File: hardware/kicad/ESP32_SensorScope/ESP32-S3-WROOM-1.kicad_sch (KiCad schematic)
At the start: 20 parts, among them J9 USB_C_Receptacle_USB2.0_16P, SW2 Reset, SW3 Boot, U16 TLV76133DCY, U2 ESP32-S3-WROOM-1, U27 USBLC6-2SC6

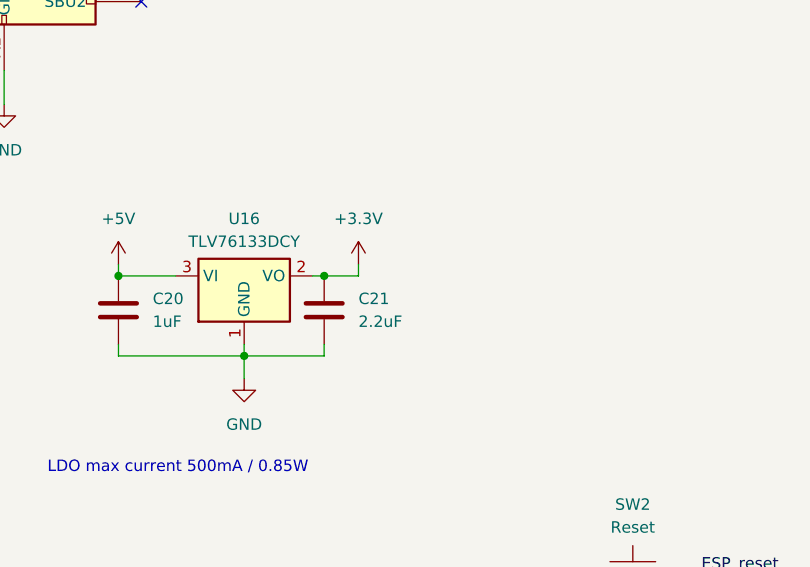
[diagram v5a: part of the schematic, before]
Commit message: addet some footprints"
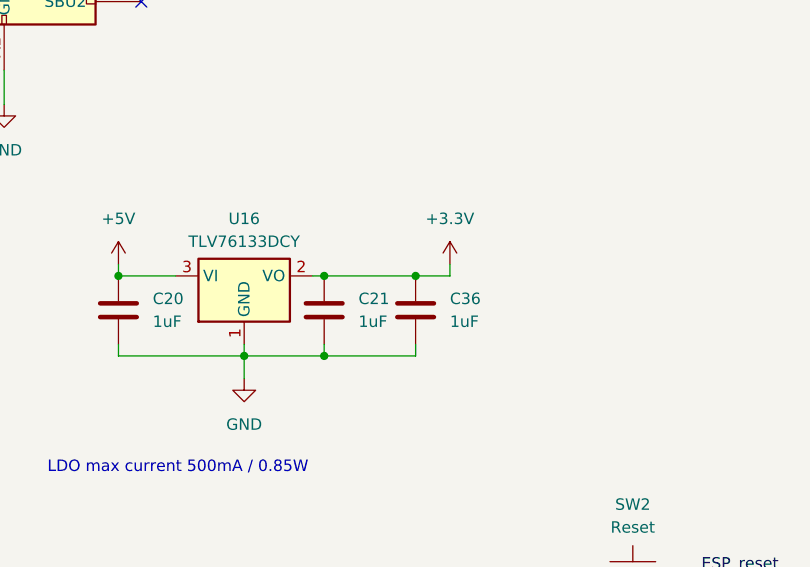
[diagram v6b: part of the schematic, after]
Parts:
- added C36: 1uF, Capacitor_SMD:C_0805_2012Metric, symbol Device:C
- C20, C22, C24: footprint (none) -> Capacitor_SMD:C_0805_2012Metric
- C21: value 2.2uF -> 1uF; footprint (none) -> Capacitor_SMD:C_0805_2012Metric
- C23: footprint (none) -> Capacitor_SMD:C_1206_3216Metric
- D11: footprint (none) -> Diode_SMD:D_SMA
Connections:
- net +3.3V: now also C36.1
- net GND: now also C36.2
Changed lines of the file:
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@@
 	(paper "A4")
 	(junction
+		(at 87.63 110.49)
+		(diameter 0)
+		(color 0 0 0 0)
+	)
+	(junction
 		(at 58.42 64.77)
 		(diameter 0)
@@
 	)
 	(junction
+		(at 77.47 119.38)
+		(diameter 0)
+		(color 0 0 0 0)
+	)
+	(junction
 		(at 77.47 110.49)
 		(diameter 0)
@@
 	(wire
 		(pts
-			(xy 77.47 110.49) (xy 81.28 110.49)
+			(xy 110.49 25.4) (xy 110.49 27.94)
 		)
 		(stroke
@@
 	(wire
 		(pts
-			(xy 110.49 25.4) (xy 110.49 27.94)
+			(xy 87.63 118.11) (xy 87.63 119.38)
+		)
+		(stroke
+			(width 0)
+			(type default)
+		)
+	)
+	(wire
+		(pts
+			(xy 87.63 119.38) (xy 77.47 119.38)
 		)
 		(stroke
@@
 	(wire
 		(pts
-			(xy 81.28 110.49) (xy 81.28 109.22)
+			(xy 91.44 110.49) (xy 91.44 109.22)
 		)
 		(stroke
@@
 	(wire
 		(pts
+			(xy 87.63 110.49) (xy 91.44 110.49)
+		)
+		(stroke
+			(width 0)
+			(type default)
+		)
+	)
+	(wire
+		(pts
 			(xy 72.39 40.64) (xy 69.85 40.64)
 		)
@@
 	(wire
 		(pts
+			(xy 77.47 110.49) (xy 87.63 110.49)
+		)
+		(stroke
+			(width 0)
+			(type default)
+		)
+	)
+	(wire
+		(pts
 			(xy 57.15 57.15) (xy 58.42 57.15)
 		)
@@
 			)
 		)
-		(property "Footprint" ""
+		(property "Footprint" "Capacitor_SMD:C_0805_2012Metric"
 			(at 177.4952 27.94 0)
 			(effects
@@
 			)
 		)
-		(property "Footprint" ""
+		(property "Footprint" "Capacitor_SMD:C_1206_3216Metric"
 			(at 164.7952 27.94 0)
 			(effects
@@
 			)
 		)
-		(property "Footprint" ""
+		(property "Footprint" "Capacitor_SMD:C_0805_2012Metric"
 			(at 55.5752 118.11 0)
 			(effects
@@
 	(symbol
 		(lib_id "power:+3.3V")
-		(at 81.28 109.22 0)
+		(at 91.44 109.22 0)
 		(unit 1)
 		(exclude_from_sim no)
@@
 		(fields_autoplaced yes)
 		(property "Reference" "#PWR069"
-			(at 81.28 113.03 0)
+			(at 91.44 113.03 0)
 			(effects
 				(font
@@
 		)
 		(property "Value" "+3.3V"
-			(at 81.28 104.14 0)
+			(at 91.44 104.14 0)
 			(effects
 				(font
@@
 		)
 		(property "Footprint" ""
-			(at 81.28 109.22 0)
+			(at 91.44 109.22 0)
 			(effects
 				(font
@@
 		)
 		(property "Datasheet" ""
-			(at 81.28 109.22 0)
+			(at 91.44 109.22 0)
 			(effects
 				(font
@@
 		)
 		(property "Description" "Power symbol creates a global label with name \"+3.3V\""
-			(at 81.28 109.22 0)
+			(at 91.44 109.22 0)
 			(effects
 				(font
@@
 			)
 		)
-		(property "Footprint" ""
+		(property "Footprint" "Diode_SMD:D_SMA"
 			(at 74.93 49.53 0)
 			(effects
@@
 			)
 		)
-		(property "Value" "2.2uF"
+		(property "Value" "1uF"
 			(at 81.28 115.5699 0)
 			(effects
@@
 			)
 		)
-		(property "Footprint" ""
+		(property "Footprint" "Capacitor_SMD:C_0805_2012Metric"
 			(at 78.4352 118.11 0)
 			(effects
@@
 			)
 		)
-		(property "Footprint" ""
+		(property "Footprint" "Capacitor_SMD:C_0805_2012Metric"
 			(at 111.4552 44.45 0)
 			(effects
@@
 					(unit 1)
 				)
+			)
+		)
+	)
+	(symbol
+		(lib_id "Device:C")
+		(at 87.63 114.3 0)
+		(unit 1)
+		(exclude_from_sim no)
+		(in_bom yes)
+		(on_board yes)
+		(dnp no)
+		(fields_autoplaced yes)
+		(property "Reference" "C36"
+			(at 91.44 113.0299 0)
+			(effects
+				(font
+					(size 1.27 1.27)
+				)
+				(justify left)
+			)
+		)
+		(property "Value" "1uF"
+			(at 91.44 115.5699 0)
+			(effects
+				(font
+					(size 1.27 1.27)
+				)
+				(justify left)
+			)
+		)
+		(property "Footprint" "Capacitor_SMD:C_0805_2012Metric"
+			(at 88.5952 118.11 0)
+			(effects
+				(font
+					(size 1.27 1.27)
+				)
+				(hide yes)
+			)
+		)
+		(property "Datasheet" "~"
+			(at 87.63 114.3 0)
+			(effects
+				(font
+					(size 1.27 1.27)
+				)
+				(hide yes)
+			)
+		)
+		(property "Description" "Unpolarized capacitor"
+			(at 87.63 114.3 0)
+			(effects
+				(font
+					(size 1.27 1.27)
+				)
+				(hide yes)
+			)
+		)
+		(pin "1"
+		)
+		(pin "2"
+		)
+		(instances
+			(project "ESP32_SensorScope"
+				(path "/53b18f60-802b-4114-ad1b-2672cfed64a1/d42b7ebf-ab51-4684-9781-2f92117935ee"
+					(reference "C36")
+					(unit 1)
+				)
